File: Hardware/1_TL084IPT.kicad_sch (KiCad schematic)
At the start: 34 parts

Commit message: after merge dev
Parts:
- gave numbers to parts that had none: 30

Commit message: add R0603 footprint
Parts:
- C17: footprint (none) -> IVS_FOOTPRINTS:C0603
- R26, R27, R28, R29, R30, R31, R32, R33, R34, R35, R36, R37, R38, R39, R40, R41: footprint (none) -> IVS_FOOTPRINTS:R0603
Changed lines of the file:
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@@
       (effects (font (size 1.27 1.27)) (justify left))
     )
-    (property "Footprint" "" (id 2) (at 59.182 91.44 90)
+    (property "Footprint" "IVS_FOOTPRINTS:R0603" (id 2) (at 59.182 91.44 90)
       (effects (font (size 1.27 1.27)) hide)
     )
@@
       (effects (font (size 1.27 1.27)) (justify left))
     )
-    (property "Footprint" "" (id 2) (at 92.202 52.07 90)
+    (property "Footprint" "IVS_FOOTPRINTS:R0603" (id 2) (at 92.202 52.07 90)
       (effects (font (size 1.27 1.27)) hide)
     )
@@
       (effects (font (size 1.27 1.27)) (justify left))
     )
-    (property "Footprint" "" (id 2) (at 117.602 171.45 90)
+    (property "Footprint" "IVS_FOOTPRINTS:R0603" (id 2) (at 117.602 171.45 90)
       (effects (font (size 1.27 1.27)) hide)
     )
@@
       (effects (font (size 1.27 1.27)) (justify left))
     )
-    (property "Footprint" "" (id 2) (at 117.602 36.83 90)
+    (property "Footprint" "IVS_FOOTPRINTS:R0603" (id 2) (at 117.602 36.83 90)
       (effects (font (size 1.27 1.27)) hide)
     )
@@
       (effects (font (size 1.27 1.27)) (justify left))
     )
-    (property "Footprint" "" (id 2) (at 59.182 180.34 90)
+    (property "Footprint" "IVS_FOOTPRINTS:R0603" (id 2) (at 59.182 180.34 90)
       (effects (font (size 1.27 1.27)) hide)
     )
@@
       (effects (font (size 1.27 1.27)) (justify left))
     )
-    (property "Footprint" "" (id 2) (at 92.202 186.69 90)
+    (property "Footprint" "IVS_FOOTPRINTS:R0603" (id 2) (at 92.202 186.69 90)
       (effects (font (size 1.27 1.27)) hide)
     )
@@
       (effects (font (size 1.27 1.27)) (justify left))
     )
-    (property "Footprint" "" (id 2) (at 117.602 125.73 90)
+    (property "Footprint" "IVS_FOOTPRINTS:R0603" (id 2) (at 117.602 125.73 90)
       (effects (font (size 1.27 1.27)) hide)
     )
@@
       (effects (font (size 1.27 1.27)) (justify left))
     )
-    (property "Footprint" "" (id 2) (at 70.612 45.72 90)
+    (property "Footprint" "IVS_FOOTPRINTS:R0603" (id 2) (at 70.612 45.72 90)
       (effects (font (size 1.27 1.27)) hide)
     )
@@
       (effects (font (size 1.27 1.27)) (justify left))
     )
-    (property "Footprint" "" (id 2) (at 70.612 135.89 90)
+    (property "Footprint" "IVS_FOOTPRINTS:R0603" (id 2) (at 70.612 135.89 90)
       (effects (font (size 1.27 1.27)) hide)
     )
@@
       (effects (font (size 1.27 1.27)) (justify left))
     )
-    (property "Footprint" "" (id 2) (at 92.202 97.79 90)
+    (property "Footprint" "IVS_FOOTPRINTS:R0603" (id 2) (at 92.202 97.79 90)
       (effects (font (size 1.27 1.27)) hide)
     )
@@
       (effects (font (size 1.27 1.27)) (justify left))
     )
-    (property "Footprint" "" (id 2) (at 59.182 135.89 90)
+    (property "Footprint" "IVS_FOOTPRINTS:R0603" (id 2) (at 59.182 135.89 90)
       (effects (font (size 1.27 1.27)) hide)
     )
@@
       (effects (font (size 1.27 1.27)) (justify left))
     )
-    (property "Footprint" "" (id 2) (at 87.3252 33.02 0)
+    (property "Footprint" "IVS_FOOTPRINTS:C0603" (id 2) (at 87.3252 33.02 0)
       (effects (font (size 1.27 1.27)) hide)
     )
@@
       (effects (font (size 1.27 1.27)) (justify left))
     )
-    (property "Footprint" "" (id 2) (at 59.182 45.72 90)
+    (property "Footprint" "IVS_FOOTPRINTS:R0603" (id 2) (at 59.182 45.72 90)
       (effects (font (size 1.27 1.27)) hide)
     )
@@
       (effects (font (size 1.27 1.27)) (justify left))
     )
-    (property "Footprint" "" (id 2) (at 70.612 180.34 90)
+    (property "Footprint" "IVS_FOOTPRINTS:R0603" (id 2) (at 70.612 180.34 90)
       (effects (font (size 1.27 1.27)) hide)
     )
@@
       (effects (font (size 1.27 1.27)) (justify left))
     )
-    (property "Footprint" "" (id 2) (at 117.602 82.55 90)
+    (property "Footprint" "IVS_FOOTPRINTS:R0603" (id 2) (at 117.602 82.55 90)
       (effects (font (size 1.27 1.27)) hide)
     )
@@
       (effects (font (size 1.27 1.27)) (justify left))
     )
-    (property "Footprint" "" (id 2) (at 92.202 140.97 90)
+    (property "Footprint" "IVS_FOOTPRINTS:R0603" (id 2) (at 92.202 140.97 90)
       (effects (font (size 1.27 1.27)) hide)
     )
@@
       (effects (font (size 1.27 1.27)) (justify left))
     )
-    (property "Footprint" "" (id 2) (at 70.612 91.44 90)
-      (effects (font (size 1.27 1.27)) hide)
-    )
+    (property "Footprint" "IVS_FOOTPRINTS:R0603" (id 2) (at 70.612 91.44 90)
+      (effects (font (size 1.27 1.27)) hide)
+    )

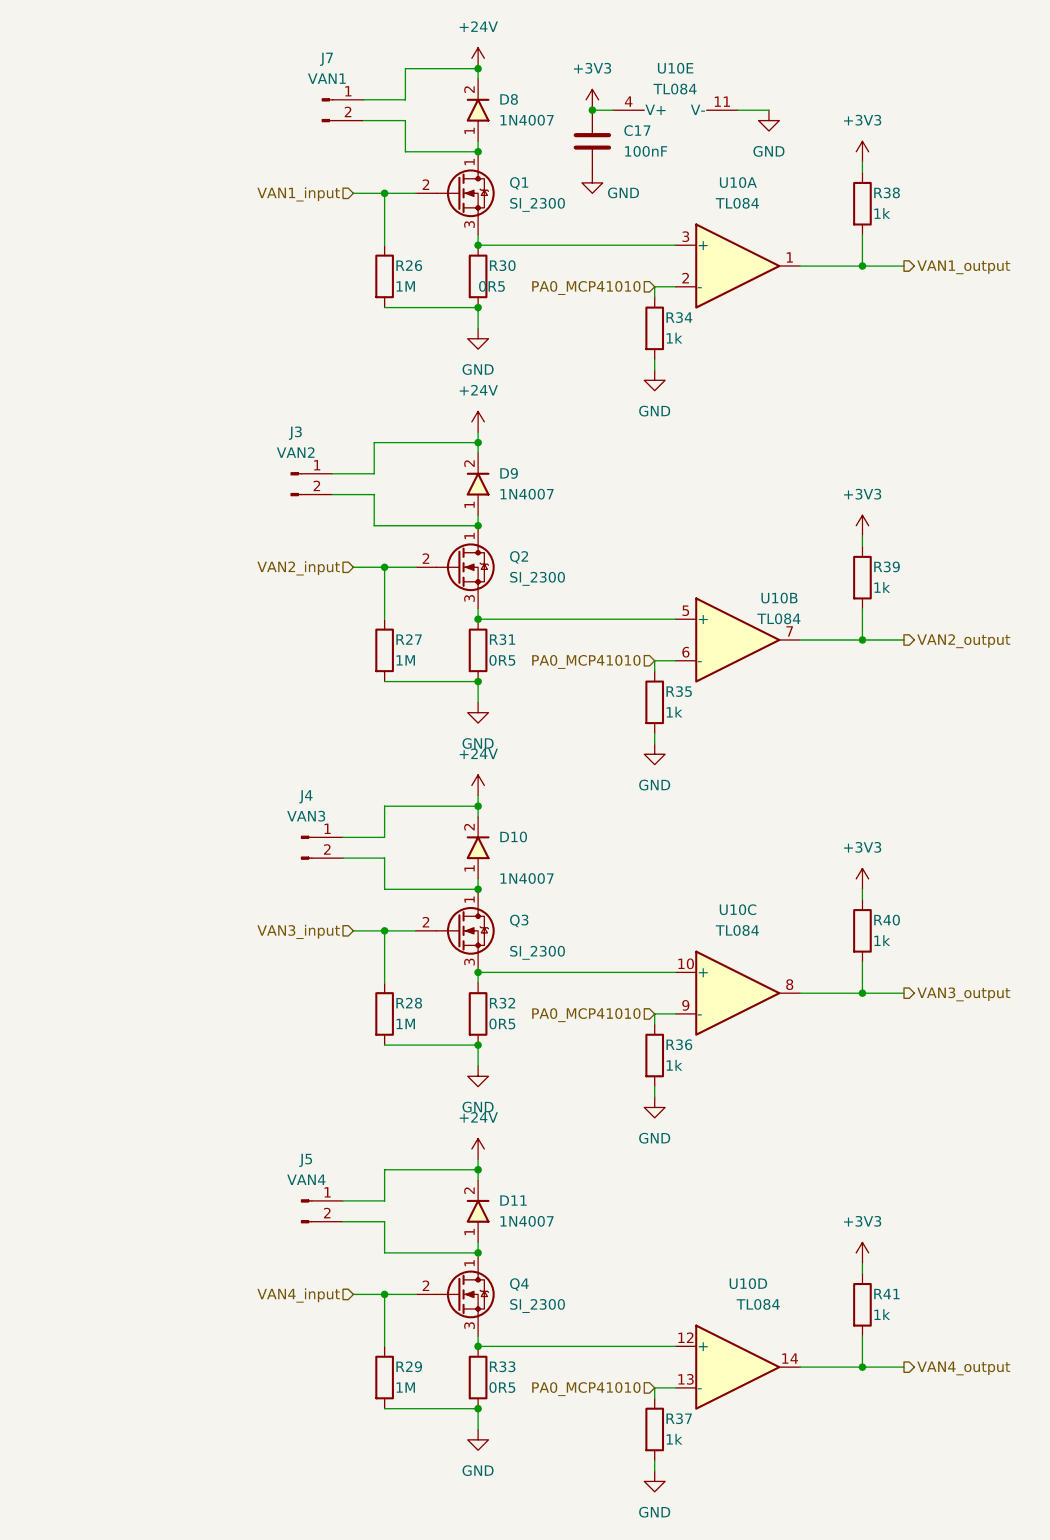
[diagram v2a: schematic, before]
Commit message: fix MCP41010, fix symbol output header
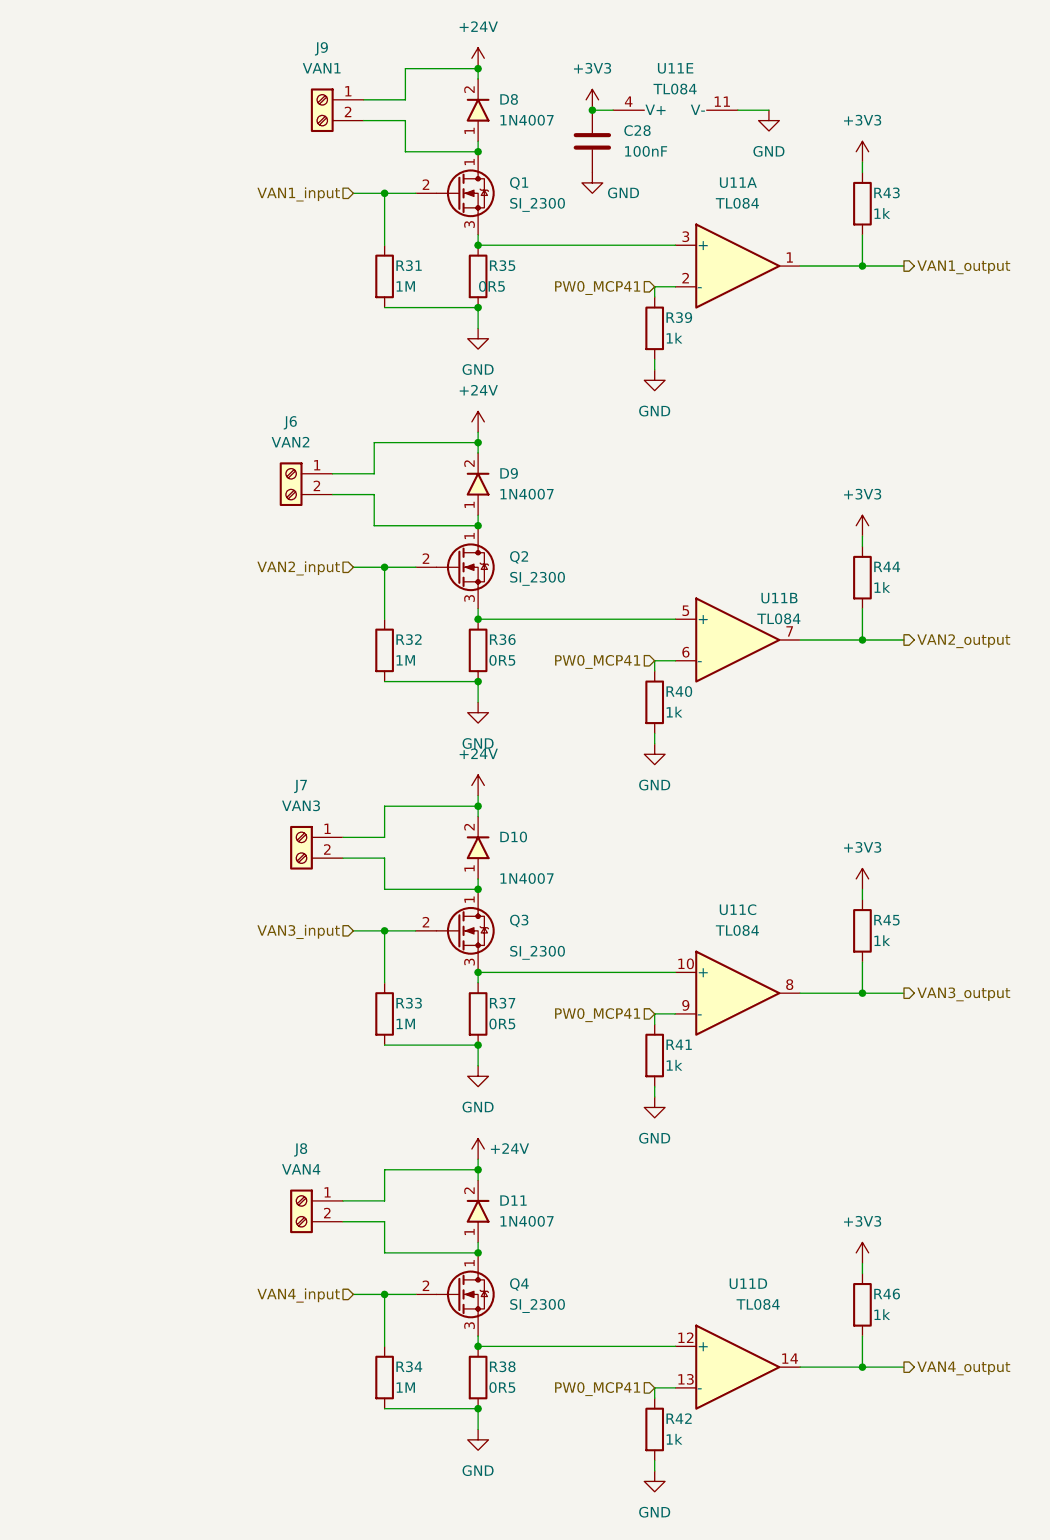
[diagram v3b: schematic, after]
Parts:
- J6: renamed from J3; symbol Connector:Conn_01x02_Male -> Connector:Screw_Terminal_01x02
- J7: renamed from J4; symbol Connector:Conn_01x02_Male -> Connector:Screw_Terminal_01x02
- J8: renamed from J5; symbol Connector:Conn_01x02_Male -> Connector:Screw_Terminal_01x02
- J9: renamed from J7; symbol Connector:Conn_01x02_Male -> Connector:Screw_Terminal_01x02
- R35: renamed from R30; footprint IVS_FOOTPRINTS:R0603 -> Resistor_SMD:R_0805_2012Metric
- R36: renamed from R31; footprint IVS_FOOTPRINTS:R0603 -> Resistor_SMD:R_0805_2012Metric
- R37: renamed from R32; footprint IVS_FOOTPRINTS:R0603 -> Resistor_SMD:R_0805_2012Metric
- R38: renamed from R33; footprint IVS_FOOTPRINTS:R0603 -> Resistor_SMD:R_0805_2012Metric
- renumbered C17 to C28, R26 to R31, R27 to R32, R28 to R33, R29 to R34, R34 to R39, R35 to R40, R36 to R41, R37 to R42, R38 to R43, R39 to R44, R40 to R45, R41 to R46, U10 to U11
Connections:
- net PA0_MCP41010 renamed PW0_MCP41

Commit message: add footprint
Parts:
- removed J6: VAN2, symbol Connector:Screw_Terminal_01x02
- removed J7: VAN3, symbol Connector:Screw_Terminal_01x02
- removed J8: VAN4, symbol Connector:Screw_Terminal_01x02
- removed J9: VAN1, symbol Connector:Screw_Terminal_01x02
- added J?: Screw_Terminal_01x08, IVS_FOOTPRINTS:HT-3.96mm, symbol Connector:Screw_Terminal_01x08
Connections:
- net +24V: now also J?.1 (Pin_1), J?.3 (Pin_3), J?.5 (Pin_5), J?.7 (Pin_7)
- net VAN4-: now reaches D11.1, Q4.1 (D)
- net VAN4-: now also J?.8 (Pin_8)
- net VAN3-: now reaches D10.1, Q3.1 (D)
- net VAN3-: now also J?.6 (Pin_6)
- net VAN1-: now reaches D8.1, Q1.1 (D)
- net VAN1-: now also J?.2 (Pin_2)
- net VAN2-: now reaches D9.1, Q2.1 (D)
- net VAN2-: now also J?.4 (Pin_4)
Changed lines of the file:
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@@
+    (stroke (width 0) (type default) (color 0 0 0 0))
+  )
+  (wire (pts (xy 60.96 176.53) (xy 60.96 170.18))
+    (stroke (width 0) (type default) (color 0 0 0 0))
+  )
+  (wire (pts (xy 93.98 181.61) (xy 96.52 181.61))
+    (stroke (width 0) (type default) (color 0 0 0 0))
+  )
+  (wire (pts (xy 72.39 154.94) (xy 72.39 156.21))
+    (stroke (width 0) (type default) (color 0 0 0 0))
+  )
+  (wire (pts (xy 72.39 139.7) (xy 72.39 142.24))
+    (stroke (width 0) (type default) (color 0 0 0 0))
+  )
+  (wire (pts (xy 72.39 176.53) (xy 96.52 176.53))
+    (stroke (width 0) (type default) (color 0 0 0 0))
+  )
+  (wire (pts (xy 60.96 95.25) (xy 72.39 95.25))
+    (stroke (width 0) (type default) (color 0 0 0 0))
+  )
+  (wire (pts (xy 72.39 74.93) (xy 72.39 76.2))
+    (stroke (width 0) (type default) (color 0 0 0 0))
+  )
+  (wire (pts (xy 93.98 92.71) (xy 96.52 92.71))
+    (stroke (width 0) (type default) (color 0 0 0 0))
+  )
+  (wire (pts (xy 93.98 135.89) (xy 96.52 135.89))
+    (stroke (width 0) (type default) (color 0 0 0 0))
+  )
+  (wire (pts (xy 60.96 125.73) (xy 64.77 125.73))
+    (stroke (width 0) (type default) (color 0 0 0 0))
+  )
+  (wire (pts (xy 60.96 35.56) (xy 64.77 35.56))
+    (stroke (width 0) (type default) (color 0 0 0 0))
+  )
+  (wire (pts (xy 111.76 133.35) (xy 119.38 133.35))
+    (stroke (width 0) (type default) (color 0 0 0 0))
+  )
+  (wire (pts (xy 60.96 114.3) (xy 60.96 110.49))
+    (stroke (width 0) (type default) (color 0 0 0 0))
+  )
+  (wire (pts (xy 60.96 139.7) (xy 72.39 139.7))
+    (stroke (width 0) (type default) (color 0 0 0 0))
+  )
+  (wire (pts (xy 119.38 129.54) (xy 119.38 133.35))
+    (stroke (width 0) (type default) (color 0 0 0 0))
+  )
+  (wire (pts (xy 72.39 86.36) (xy 72.39 87.63))
+    (stroke (width 0) (type default) (color 0 0 0 0))
+  )
+  (wire (pts (xy 60.96 165.1) (xy 72.39 165.1))
+    (stroke (width 0) (type default) (color 0 0 0 0))
+  )
+  (wire (pts (xy 93.98 102.87) (xy 93.98 101.6))
+    (stroke (width 0) (type default) (color 0 0 0 0))
+  )
+  (wire (pts (xy 60.96 132.08) (xy 60.96 125.73))
     (stroke (width 0) (type default) (color 0 0 0 0))
   )
@@
     (stroke (width 0) (type default) (color 0 0 0 0))
   )
-  (wire (pts (xy 60.96 176.53) (xy 60.96 170.18))
-    (stroke (width 0) (type default) (color 0 0 0 0))
-  )
-  (wire (pts (xy 93.98 181.61) (xy 96.52 181.61))
-    (stroke (width 0) (type default) (color 0 0 0 0))
-  )
-  (wire (pts (xy 72.39 154.94) (xy 72.39 156.21))
-    (stroke (width 0) (type default) (color 0 0 0 0))
-  )
-  (wire (pts (xy 72.39 139.7) (xy 72.39 142.24))
-    (stroke (width 0) (type default) (color 0 0 0 0))
-  )
-  (wire (pts (xy 72.39 176.53) (xy 96.52 176.53))
-    (stroke (width 0) (type default) (color 0 0 0 0))
-  )
-  (wire (pts (xy 60.96 95.25) (xy 72.39 95.25))
-    (stroke (width 0) (type default) (color 0 0 0 0))
-  )
-  (wire (pts (xy 72.39 74.93) (xy 72.39 76.2))
-    (stroke (width 0) (type default) (color 0 0 0 0))
-  )
-  (wire (pts (xy 93.98 92.71) (xy 96.52 92.71))
-    (stroke (width 0) (type default) (color 0 0 0 0))
-  )
-  (wire (pts (xy 93.98 135.89) (xy 96.52 135.89))
-    (stroke (width 0) (type default) (color 0 0 0 0))
-  )
-  (wire (pts (xy 60.96 125.73) (xy 64.77 125.73))
-    (stroke (width 0) (type default) (color 0 0 0 0))
-  )
-  (wire (pts (xy 60.96 35.56) (xy 64.77 35.56))
-    (stroke (width 0) (type default) (color 0 0 0 0))
-  )
-  (wire (pts (xy 111.76 133.35) (xy 119.38 133.35))
-    (stroke (width 0) (type default) (color 0 0 0 0))
-  )
-  (wire (pts (xy 60.96 114.3) (xy 60.96 110.49))
-    (stroke (width 0) (type default) (color 0 0 0 0))
-  )
-  (wire (pts (xy 60.96 139.7) (xy 72.39 139.7))
-    (stroke (width 0) (type default) (color 0 0 0 0))
-  )
-  (wire (pts (xy 119.38 129.54) (xy 119.38 133.35))
-    (stroke (width 0) (type default) (color 0 0 0 0))
-  )
-  (wire (pts (xy 72.39 86.36) (xy 72.39 87.63))
-    (stroke (width 0) (type default) (color 0 0 0 0))
-  )
-  (wire (pts (xy 60.96 165.1) (xy 72.39 165.1))
-    (stroke (width 0) (type default) (color 0 0 0 0))
-  )
-  (wire (pts (xy 93.98 102.87) (xy 93.98 101.6))
-    (stroke (width 0) (type default) (color 0 0 0 0))
-  )
-  (wire (pts (xy 60.96 132.08) (xy 60.96 125.73))
-    (stroke (width 0) (type default) (color 0 0 0 0))
-  )
   (wire (pts (xy 63.5 30.48) (xy 72.39 30.48))
     (stroke (width 0) (type default) (color 0 0 0 0))
@@
   (wire (pts (xy 60.96 81.28) (xy 64.77 81.28))
     (stroke (width 0) (type default) (color 0 0 0 0))
+  )
+  (label "VAN2-" (at 54.61 72.39 0)
+    (effects (font (size 1.27 1.27)) (justify left bottom))
+  )
+  (label "VAN1+" (at 58.42 24.13 0)
+    (effects (font (size 1.27 1.27)) (justify left bottom))
+  )
+  (label "VAN3+" (at 55.88 114.3 0)
+    (effects (font (size 1.27 1.27)) (justify left bottom))
+  )
+  (label "VAN1+" (at 33.655 95.885 0)
+    (effects (font (size 1.27 1.27)) (justify left bottom))
+  )
+  (label "VAN4-" (at 55.88 161.29 0)
+    (effects (font (size 1.27 1.27)) (justify left bottom))
+  )
+  (label "VAN4-" (at 33.655 113.665 0)
+    (effects (font (size 1.27 1.27)) (justify left bottom))
+  )
+  (label "VAN2-" (at 33.655 103.505 0)
+    (effects (font (size 1.27 1.27)) (justify left bottom))
+  )
+  (label "VAN4+" (at 55.88 158.75 0)
+    (effects (font (size 1.27 1.27)) (justify left bottom))
+  )
+  (label "VAN3-" (at 55.88 116.84 0)
+    (effects (font (size 1.27 1.27)) (justify left bottom))
+  )
+  (label "VAN4+" (at 33.655 111.125 0)
+    (effects (font (size 1.27 1.27)) (justify left bottom))
+  )
+  (label "VAN2+" (at 54.61 69.85 0)
+    (effects (font (size 1.27 1.27)) (justify left bottom))
+  )
+  (label "VAN1-" (at 33.655 98.425 0)
+    (effects (font (size 1.27 1.27)) (justify left bottom))
+  )
+  (label "VAN2+" (at 33.655 100.965 0)
+    (effects (font (size 1.27 1.27)) (justify left bottom))
+  )
+  (label "VAN3-" (at 33.655 108.585 0)
+    (effects (font (size 1.27 1.27)) (justify left bottom))
+  )
+  (label "VAN1-" (at 58.42 26.67 0)
+    (effects (font (size 1.27 1.27)) (justify left bottom))
+  )
+  (label "VAN3+" (at 33.655 106.045 0)
+    (effects (font (size 1.27 1.27)) (justify left bottom))
   )
   (hierarchical_label "VAN2_input" (shape input) (at 57.15 81.28 180)
@@
     )
     (property "Datasheet" "~" (id 3) (at 119.38 36.83 0)
-      (effects (font (size 1.27 1.27)) hide)
-    )
-    (pin "1")
-    (pin "2")
-  )
-  (symbol (lib_id "Connector:Screw_Terminal_01x02") (at 50.8 158.75 0) (mirror y) (unit 1)
-    (in_bom yes) (on_board yes) (fields_autoplaced)
-    (property "Reference" "J8" (id 0) (at 50.8 152.4 0))
-    (property "Value" "VAN4" (id 1) (at 50.8 154.94 0))
-    (property "Footprint" "" (id 2) (at 50.8 158.75 0)
-      (effects (font (size 1.27 1.27)) hide)
-    )
-    (property "Datasheet" "~" (id 3) (at 50.8 158.75 0)
       (effects (font (size 1.27 1.27)) hide)
     )
@@
     (pin "1")
   )
-  (symbol (lib_id "Connector:Screw_Terminal_01x02") (at 50.8 114.3 0) (mirror y) (unit 1)
-    (in_bom yes) (on_board yes) (fields_autoplaced)
-    (property "Reference" "J7" (id 0) (at 50.8 107.95 0))
-    (property "Value" "VAN3" (id 1) (at 50.8 110.49 0))
-    (property "Footprint" "" (id 2) (at 50.8 114.3 0)
-      (effects (font (size 1.27 1.27)) hide)
-    )
-    (property "Datasheet" "~" (id 3) (at 50.8 114.3 0)
-      (effects (font (size 1.27 1.27)) hide)
-    )
-    (pin "1")
-    (pin "2")
-  )
   (symbol (lib_id "Device:R") (at 60.96 180.34 0) (unit 1)
     (in_bom yes) (on_board yes)
@@
     (pin "2")
   )
-  (symbol (lib_id "Connector:Screw_Terminal_01x02") (at 53.34 24.13 0) (mirror y) (unit 1)
-    (in_bom yes) (on_board yes) (fields_autoplaced)
-    (property "Reference" "J9" (id 0) (at 53.34 17.78 0))
-    (property "Value" "VAN1" (id 1) (at 53.34 20.32 0))
-    (property "Footprint" "" (id 2) (at 53.34 24.13 0)
-      (effects (font (size 1.27 1.27)) hide)
-    )
-    (property "Datasheet" "~" (id 3) (at 53.34 24.13 0)
-      (effects (font (size 1.27 1.27)) hide)
-    )
-    (pin "1")
-    (pin "2")
-  )
   (symbol (lib_id "IVS_SYMBOL_DIR:D_Diode") (at 72.39 114.3 270) (unit 1)
     (in_bom yes) (on_board yes)
@@
     (pin "1")
     (pin "2")
+  )
+  (symbol (lib_id "Connector:Screw_Terminal_01x08") (at 28.575 103.505 0) (mirror y) (unit 1)
+    (in_bom yes) (on_board yes) (fields_autoplaced)
+    (property "Reference" "J?" (id 0) (at 28.575 89.535 0))
+    (property "Value" "Screw_Terminal_01x08" (id 1) (at 28.575 92.075 0))
+    (property "Footprint" "IVS_FOOTPRINTS:HT-3.96mm" (id 2) (at 28.575 103.505 0)
+      (effects (font (size 1.27 1.27)) hide)
+    )
+    (property "Datasheet" "~" (id 3) (at 28.575 103.505 0)
+      (effects (font (size 1.27 1.27)) hide)
+    )
+    (pin "1")
+    (pin "2")
+    (pin "3")
+    (pin "4")
+    (pin "5")
+    (pin "6")
+    (pin "7")
+    (pin "8")
   )
   (symbol (lib_id "Device:Q_NMOS_DGS") (at 69.85 35.56 0) (unit 1)
@@
     (pin "1")
   )
-  (symbol (lib_id "Connector:Screw_Terminal_01x02") (at 49.53 69.85 0) (mirror y) (unit 1)
-    (in_bom yes) (on_board yes) (fields_autoplaced)
-    (property "Reference" "J6" (id 0) (at 49.53 63.5 0))
-    (property "Value" "VAN2" (id 1) (at 49.53 66.04 0))
-    (property "Footprint" "" (id 2) (at 49.53 69.85 0)
-      (effects (font (size 1.27 1.27)) hide)
-    )
-    (property "Datasheet" "~" (id 3) (at 49.53 69.85 0)
-      (effects (font (size 1.27 1.27)) hide)
-    )
-    (pin "1")
-    (pin "2")
-  )
 )
